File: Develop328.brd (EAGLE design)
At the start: 42.9 x 66 mm, 12 parts

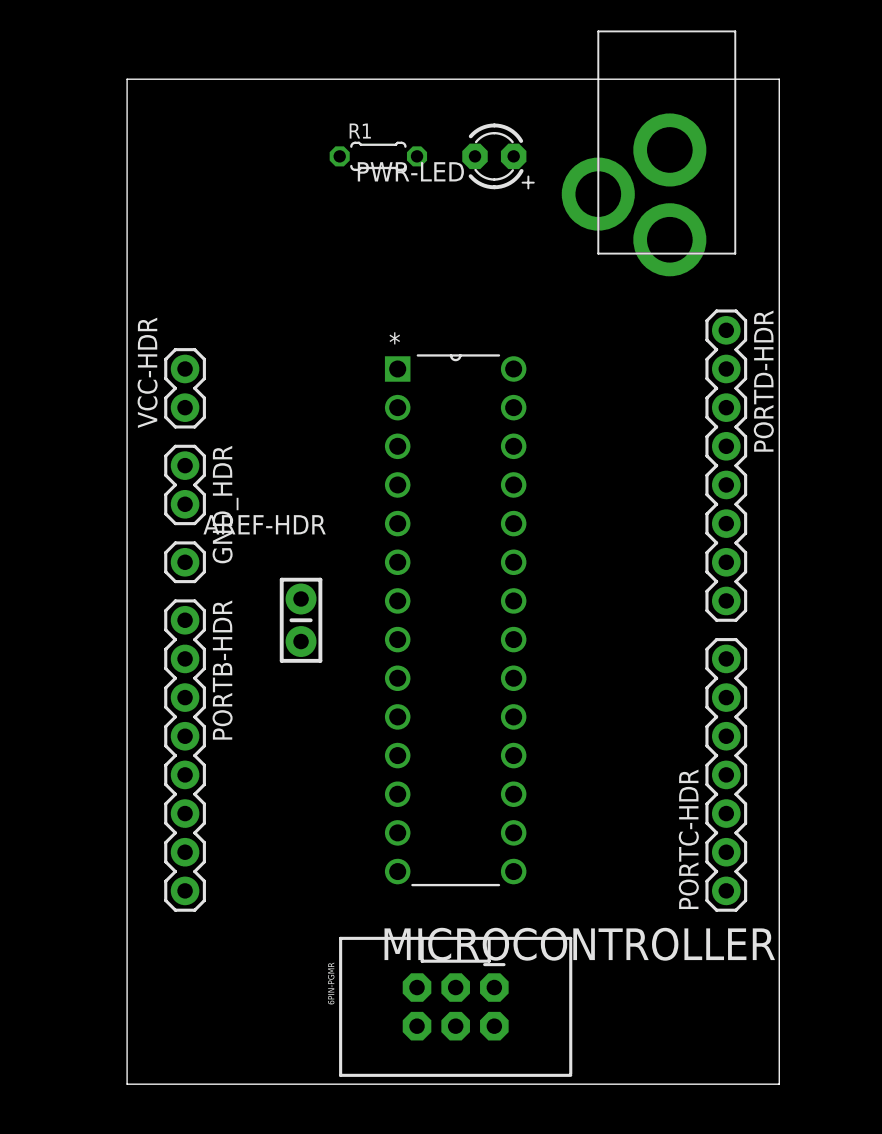
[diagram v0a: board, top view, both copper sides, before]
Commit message: Added ground plane
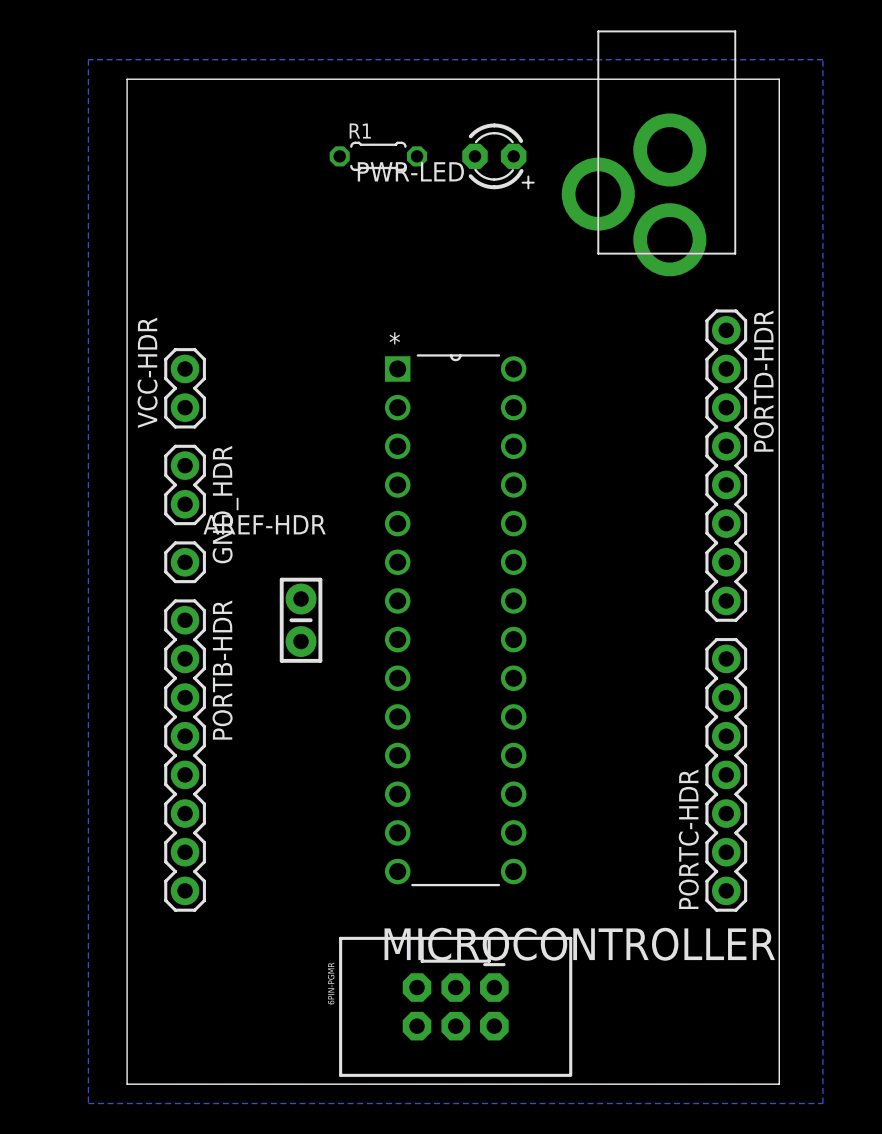
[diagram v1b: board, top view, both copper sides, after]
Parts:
- R1: value 200ohm -> 200
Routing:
- added copper zone on layer 16, net GND

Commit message: Cleaned up and added labels to board layout
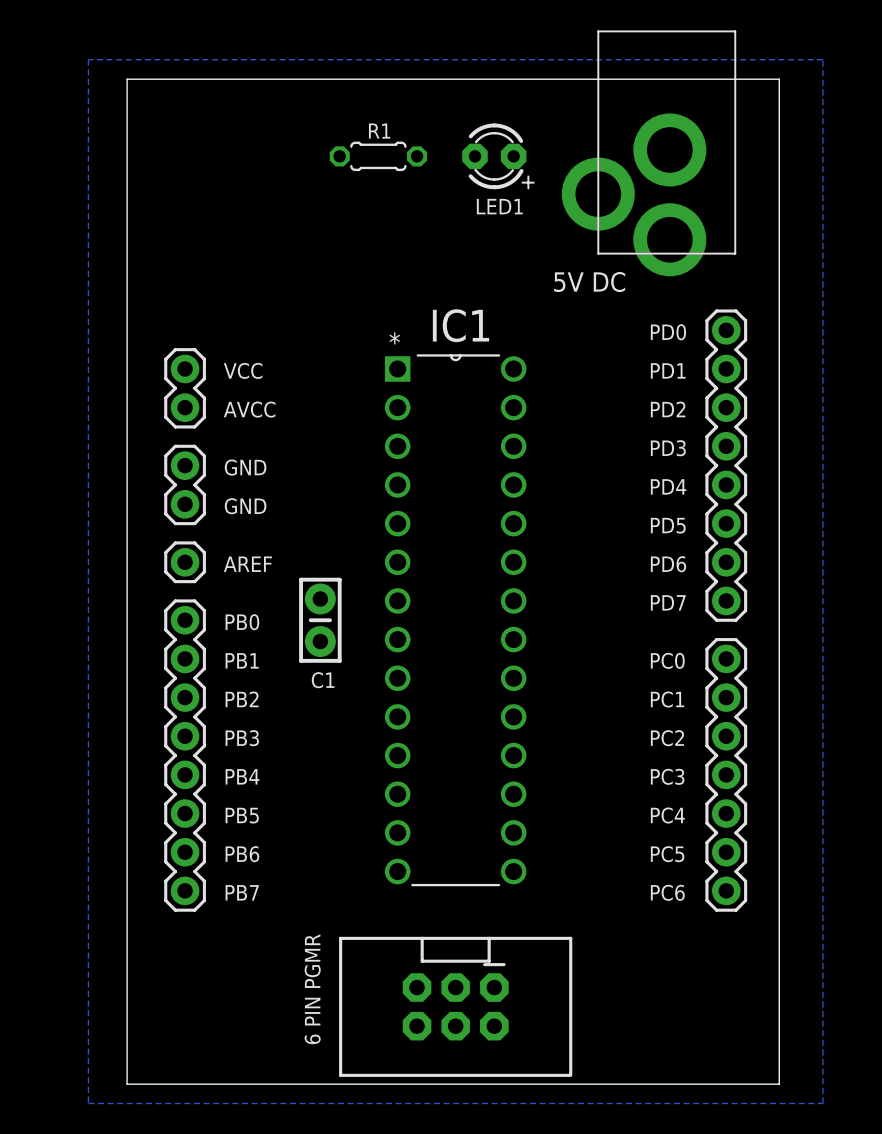
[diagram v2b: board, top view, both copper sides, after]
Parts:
- removed VCC_CAP: 0.1uF, SparkFun-Capacitors:CAP-PTH-SMALL-KIT
- added C1: 0.1uF, SparkFun-Capacitors:CAP-PTH-SMALL-KIT
- renumbered 6PIN-PGMR to PG1, MICROCONTROLLER to IC1
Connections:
- net GND: now also C1.2; no longer VCC_CAP.2
- net VCC: now also C1.1; no longer VCC_CAP.1
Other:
- board text added: "5V DC"
- board text added: "6 PIN PGMR"
- board text added: "AREF"
- board text added: "AVCC"
- board text added: "C1"
- board text added: "GND"
- board text added: "LED1"
- board text added: "PB0"
- board text added: "PB1"
- board text added: "PB2"
- board text added: "PB3"
- board text added: "PB4"
- board text added: "PB5"
- board text added: "PB6"
- board text added: "PB7"
- board text added: "PC0"
- board text added: "PC1"
- board text added: "PC2"
- board text added: "PC3"
- board text added: "PC4"
- board text added: "PC5"
- board text added: "PC6"
- board text added: "PD0"
- board text added: "PD1"
- board text added: "PD2"
- board text added: "PD3"
- board text added: "PD4"
- board text added: "PD5"
- board text added: "PD6"
- board text added: "PD7"
- board text added: "VCC"

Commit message: Added alternative functions to pin labels
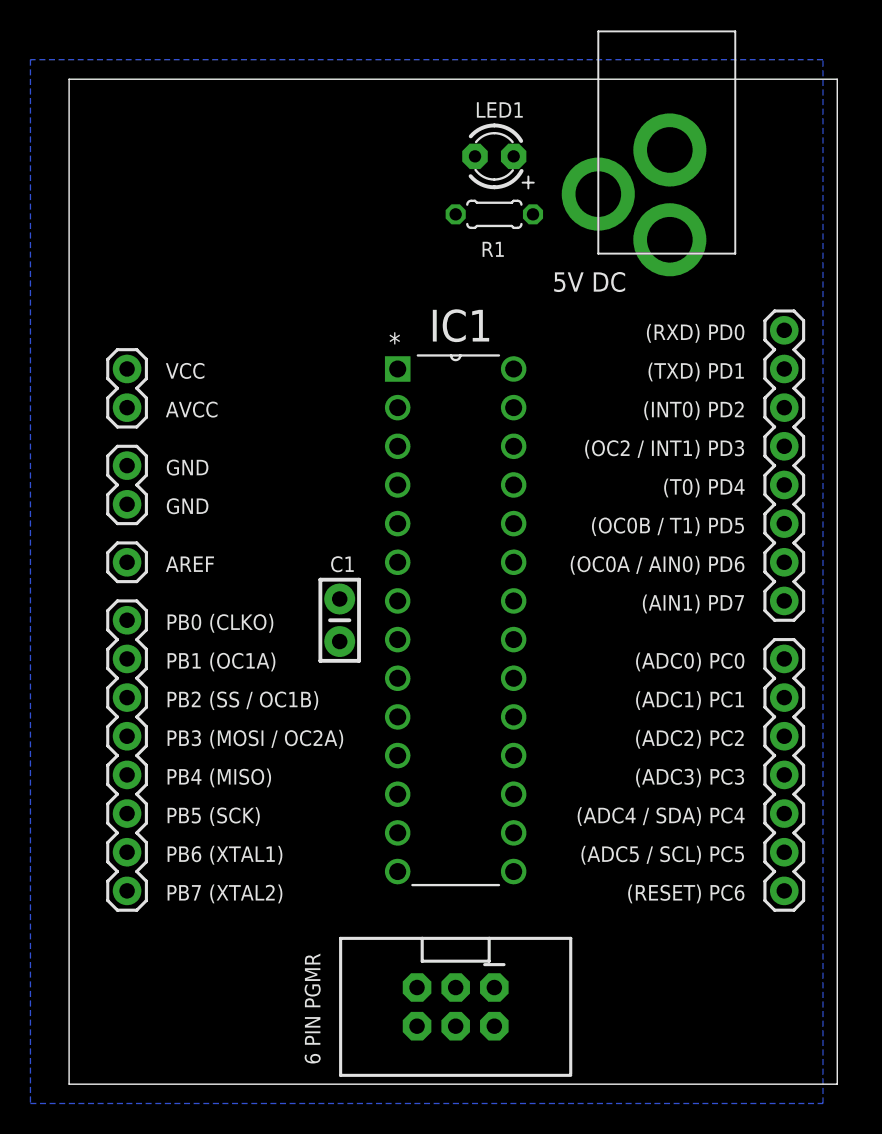
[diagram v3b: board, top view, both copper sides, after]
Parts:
- moved R1 8.52 mm to (24.1, 57.1), turned to 180 degrees
- moved PORTC-HDR 3.81 mm to (43.2, 12.7)
- moved PORTD-HDR 3.81 mm to (43.2, 49.5)
- moved AREF-HDR 3.81 mm to (0.00, 34.3)
- moved GND_HDR 3.81 mm to (0.00, 40.6)
- moved PORTB-HDR 3.81 mm to (0.00, 30.5)
- moved VCC-HDR 3.81 mm to (0.00, 44.5)
- moved C1 1.27 mm to (14.0, 30.5)
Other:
- board size 42.9 x 66 mm -> 50.5 x 66 mm
- board text added: "(ADC0) PC0"
- board text added: "(ADC1) PC1"
- board text added: "(ADC2) PC2"
- board text added: "(ADC3) PC3"
- board text added: "(ADC4 / SDA) PC4"
- board text added: "(ADC5 / SCL) PC5"
- board text added: "(AIN1) PD7"
- board text added: "(INT0) PD2"
- board text added: "(OC0A / AIN0) PD6"
- board text added: "(OC0B / T1) PD5"
- board text added: "(OC2 / INT1) PD3"
- board text added: "(RESET) PC6"
- board text added: "(RXD) PD0"
- board text added: "(T0) PD4"
- board text added: "(TXD) PD1"
- board text added: "PB0 (CLKO)"
- board text added: "PB1 (OC1A)"
- board text added: "PB2 (SS / OC1B)"
- board text added: "PB3 (MOSI / OC2A)"
- board text added: "PB4 (MISO)"
- board text added: "PB5 (SCK)"
- board text added: "PB6 (XTAL1)"
- board text added: "PB7 (XTAL2)"
- board text removed: "PB0"
- board text removed: "PB1"
- board text removed: "PB2"
- board text removed: "PB3"
- board text removed: "PB4"
- board text removed: "PB5"
- board text removed: "PB6"
- board text removed: "PB7"
- board text removed: "PC0"
- board text removed: "PC1"
- board text removed: "PC2"
- board text removed: "PC3"
- board text removed: "PC4"
- board text removed: "PC5"
- board text removed: "PC6"
- board text removed: "PD0"
- board text removed: "PD1"
- board text removed: "PD2"
- board text removed: "PD3"
- board text removed: "PD4"
- board text removed: "PD5"
- board text removed: "PD6"
- board text removed: "PD7"

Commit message: Fixed incorrect wiring for 6 pin programmer
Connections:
- removed net N$10: IC1.24, PG1.3, PORTC-HDR.2
- removed net N$11: IC1.25, PG1.5, PORTC-HDR.3
- new net N$28: IC1.25, PORTC-HDR.3
- new net N$29: IC1.24, PORTC-HDR.2
- net N$12: no longer PG1.4
- net N$5: now also PG1.5
- net N$6: now also PG1.3, PG1.4
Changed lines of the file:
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@@
 <contactref element="PORTB-HDR" pad="4"/>
 <contactref element="IC1" pad="18"/>
-<wire x1="0" y1="22.86" x2="25.4" y2="21.59" width="0" layer="19" extent="1-1"/>
+<contactref element="PG1" pad="5"/>
+<wire x1="19.05" y1="6.35" x2="25.4" y2="21.59" width="0" layer="19" extent="1-1"/>
+<wire x1="0" y1="22.86" x2="19.05" y2="6.35" width="0" layer="19" extent="1-1"/>
 </signal>
 <signal name="N$6">
 <contactref element="PORTB-HDR" pad="3"/>
 <contactref element="IC1" pad="19"/>
+<contactref element="PG1" pad="4"/>
+<contactref element="PG1" pad="3"/>
+<wire x1="21.59" y1="6.35" x2="25.4" y2="24.13" width="0" layer="19" extent="1-1"/>
+<wire x1="21.59" y1="3.81" x2="21.59" y2="6.35" width="0" layer="19" extent="1-1"/>
 <wire x1="0" y1="25.4" x2="25.4" y2="24.13" width="0" layer="19" extent="1-1"/>
 </signal>
@@
 <wire x1="43.18" y1="12.7" x2="25.4" y2="34.29" width="0" layer="19" extent="1-1"/>
 </signal>
-<signal name="N$10">
-<contactref element="PORTC-HDR" pad="2"/>
-<contactref element="IC1" pad="24"/>
-<contactref element="PG1" pad="3"/>
-<wire x1="43.18" y1="15.24" x2="25.4" y2="36.83" width="0" layer="19" extent="1-1"/>
-<wire x1="21.59" y1="6.35" x2="43.18" y2="15.24" width="0" layer="19" extent="1-1"/>
-</signal>
-<signal name="N$11">
-<contactref element="PORTC-HDR" pad="3"/>
-<contactref element="IC1" pad="25"/>
-<contactref element="PG1" pad="5"/>
-<wire x1="43.18" y1="17.78" x2="25.4" y2="39.37" width="0" layer="19" extent="1-1"/>
-<wire x1="19.05" y1="6.35" x2="43.18" y2="17.78" width="0" layer="19" extent="1-1"/>
-</signal>
 <signal name="N$12">
 <contactref element="PORTC-HDR" pad="4"/>
 <contactref element="IC1" pad="26"/>
-<contactref element="PG1" pad="4"/>
 <wire x1="43.18" y1="20.32" x2="25.4" y2="41.91" width="0" layer="19" extent="1-1"/>
-<wire x1="21.59" y1="3.81" x2="43.18" y2="20.32" width="0" layer="19" extent="1-1"/>
 </signal>
 <signal name="N$13">
@@
 <wire x1="21.59" y1="57.15" x2="22.86" y2="60.96" width="0" layer="19" extent="1-1"/>
 </signal>
+<signal name="N$28">
+<contactref element="PORTC-HDR" pad="3"/>
+<contactref element="IC1" pad="25"/>
+<wire x1="43.18" y1="17.78" x2="25.4" y2="39.37" width="0" layer="19" extent="1-1"/>
+</signal>
+<signal name="N$29">
+<contactref element="PORTC-HDR" pad="2"/>
+<contactref element="IC1" pad="24"/>
+<wire x1="43.18" y1="15.24" x2="25.4" y2="36.83" width="0" layer="19" extent="1-1"/>
+</signal>
 </signals>
